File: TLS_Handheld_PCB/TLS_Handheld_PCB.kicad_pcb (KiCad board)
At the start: 4 copper layers, 175 x 100 mm, 91 parts, among them J1 Conn_01x02_Pin, J2 Conn_01x02_Pin, J3 Conn_01x02_Pin, M1 TO-236AB_SOT23_NEX, M2 TO-236AB_SOT23_NEX, U1 LT8640SEV_PBF, U2 LT8640SEV_PBF, U3 LT8619EDD-TRPBF, U4 LAA108STR, U5 SOP65P640X110-14N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

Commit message: Added battery status circuity
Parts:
- added C_bat: 0.1uF, Capacitor_SMD:C_0805_2012Metric_Pad1.18x1.45mm_HandSolder, F.Cu at (111.5, 102.0)
- added R_2: R_0805_2012Metric_Pad1.20x1.40mm_HandSolder, Resistor_SMD:R_0805_2012Metric_Pad1.20x1.40mm_HandSolder, F.Cu at (108.5, 97.5)
- added R_bat2: R_0805_2012Metric_Pad1.20x1.40mm_HandSolder, Resistor_SMD:R_0805_2012Metric_Pad1.20x1.40mm_HandSolder, F.Cu at (111.5, 85.0)
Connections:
- STM_CN7 pad 28: (no net) -> Vbat_sense
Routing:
- net /Pin: track 32.1 -> 61.4 mm, vias 23 -> 26
- net V_bat_node: track 0.00 -> 15.2 mm
- net Vbat_sense: track 0.00 -> 8.60 mm
- net /5V: track 110.1 -> 111.2 mm
- net GND: vias 204 -> 206

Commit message: some final changes
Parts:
- added R_1: R_0805_2012Metric_Pad1.20x1.40mm_HandSolder, Resistor_SMD:R_0805_2012Metric_Pad1.20x1.40mm_HandSolder, F.Cu at (108.5, 89.5)
- moved C39 4.91 mm to (227.5, 98.5)
- moved C40 4.91 mm to (225.0, 98.5)
- moved Rref 2.61 mm to (230.0, 93.0)
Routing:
- net /3.3V: track 103.9 -> 95.9 mm
- net BIAS: track 12.0 -> 5.76 mm
- net ISENSOR: track 9.96 -> 4.46 mm
- net MOSFETGait1: track 27.2 -> 26.0 mm
- net thermDRDY: track 32.6 -> 31.8 mm
- added copper zone on In2.Cu, net GND
- removed copper zone on In2.Cu, net (none)

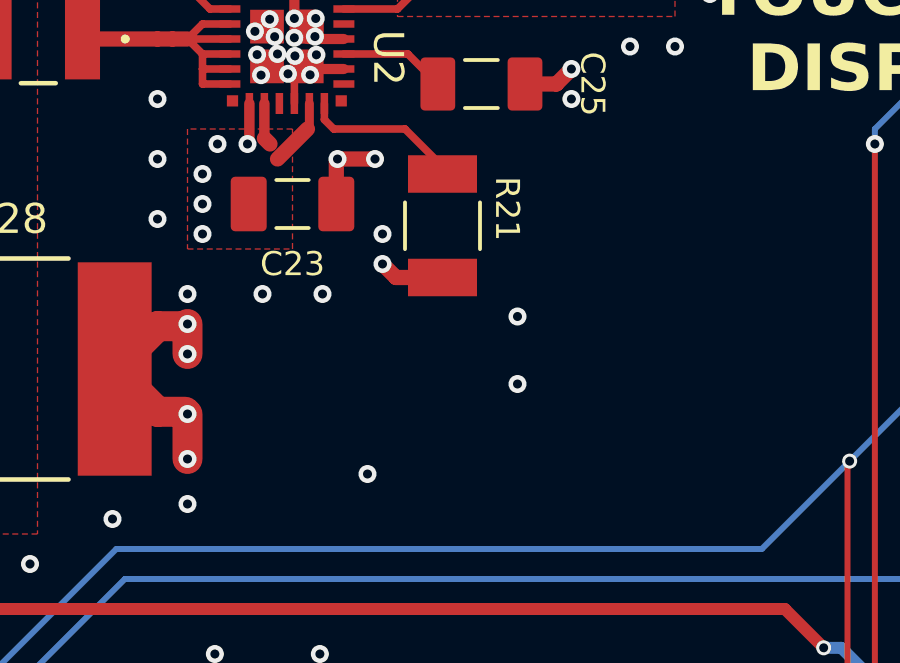
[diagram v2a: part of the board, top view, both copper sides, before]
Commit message: Delete random via
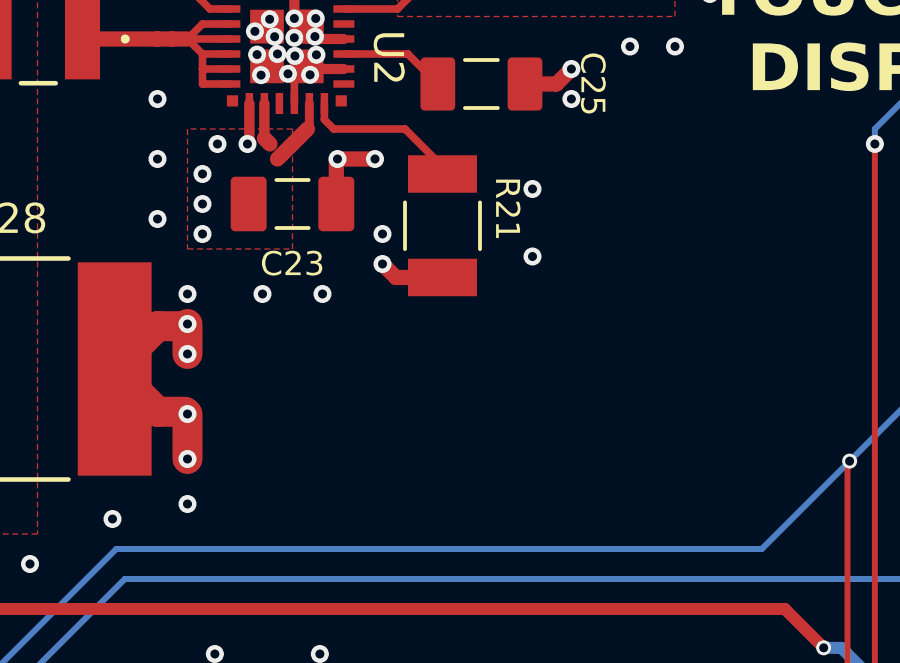
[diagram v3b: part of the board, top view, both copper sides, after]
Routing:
- net /Pin: vias 26 -> 25
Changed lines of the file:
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@@
 	)
 	(via
-		(at 139.5 97)
+		(at 140 92.75)
 		(size 0.6)
 		(drill 0.3)
@@
 	)
 	(via
-		(at 139.5 94.75)
+		(at 140 90.5)
 		(size 0.6)
 		(drill 0.3)
@@
 		(size 0.6)
 		(drill 0.3)
-		(layers "F.Cu" "B.Cu")
-		(free yes)
-		(net 52)
-	)
-	(via
-		(at 134.5 100)
-		(size 0.6)
-		(drill 0.3)

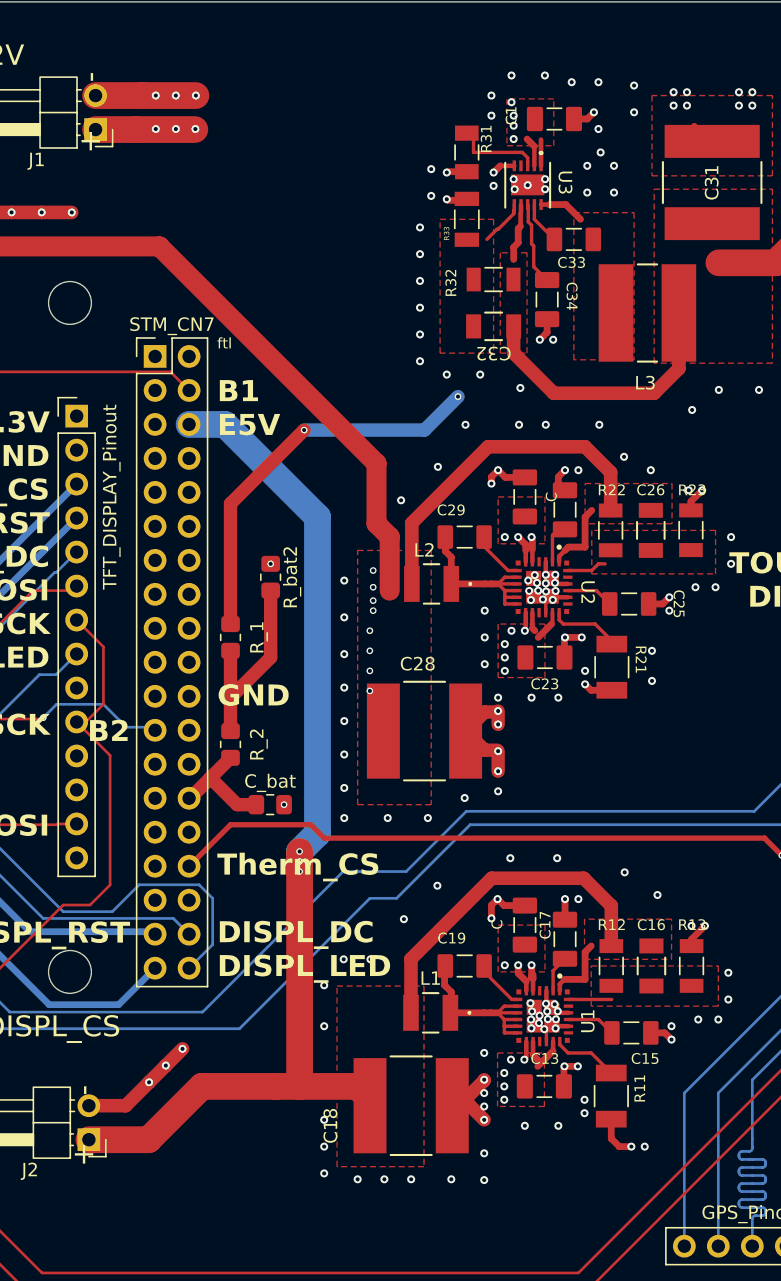
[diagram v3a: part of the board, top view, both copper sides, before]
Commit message: Add Marcs changes to inductors and traces widths.
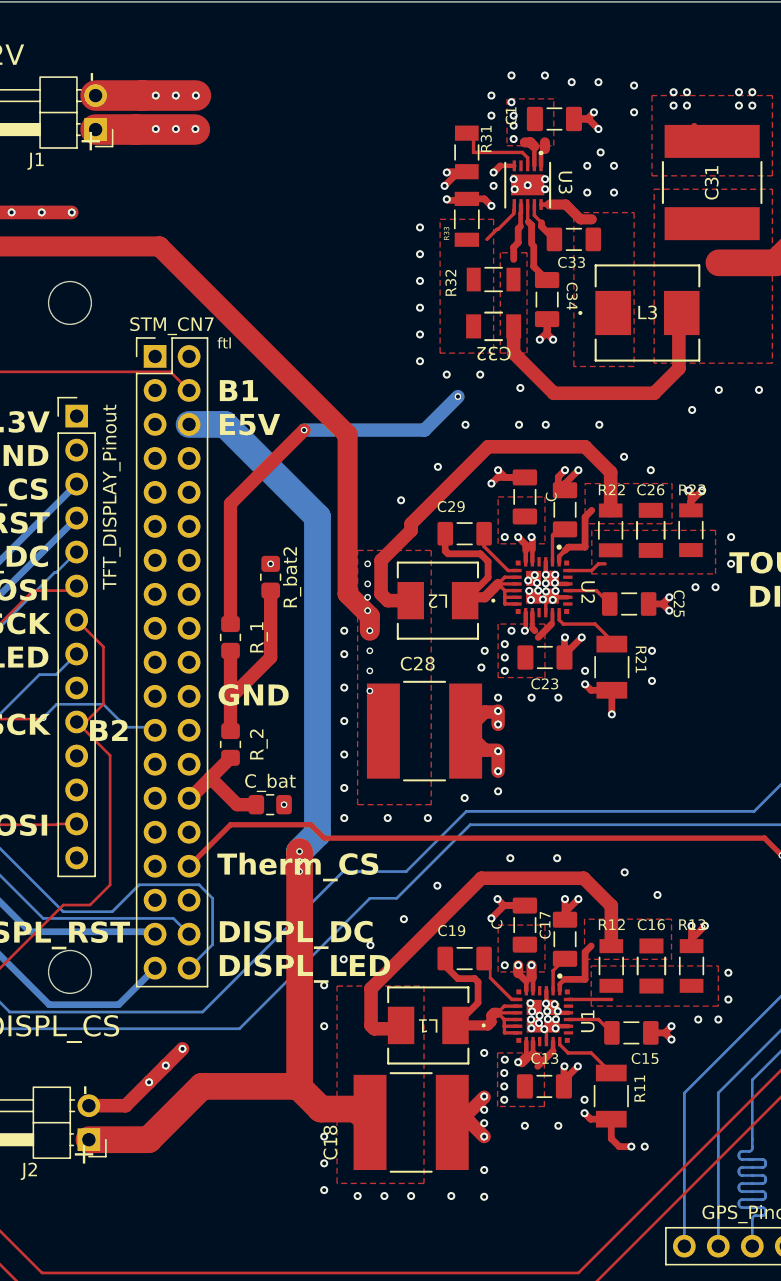
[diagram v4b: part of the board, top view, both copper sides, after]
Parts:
- L1, L2: footprint footprints55:IND_DFE322512F_MUR -> footprints 9:IND_IHLP-2020CZ
- L3: footprint footprints44:IND_BOURNS_SRR6038 -> footprints 10:IND_ASPI-0630LR_ABR
- moved L2 1.34 mm to (124.0, 86.8)
- moved C18 1.25 mm to (122.0, 125.8)
- moved L1 0.96 mm to (123.3, 118.5)
- moved C19 0.56 mm to (126.0, 113.5)
- moved C29 0.25 mm to (126.0, 81.8)
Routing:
- net GND: track 115.7 -> 140.4 mm, vias 206 -> 205
- net /3.3V: track 95.9 -> 102.4 mm
- net /5V: track 111.2 -> 116.6 mm
- net /SW1: track 15.2 -> 20.4 mm
- net /SW2: track 14.7 -> 19.2 mm
- net /SW3: track 3.43 -> 4.26 mm
- net Net-(U1-BST): track 3.60 -> 4.35 mm
- net /Pin: track 61.4 -> 61.9 mm
